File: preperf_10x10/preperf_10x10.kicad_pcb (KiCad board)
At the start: 2 copper layers, 100 x 100 mm, 72 parts, among them J1 Conn_01x02_Pin, J2 Conn_01x02_Pin, J3 Conn_01x02_Pin, J4 Conn_01x01_Pin, J5 Conn_01x01_Pin, J6 Conn_01x01_Pin, J7 Conn_01x01_Pin, J8 Conn_01x01_Pin, J9 Conn_01x01_Pin, Q1 BC548, Q2 BC558, SW1 SW_DIP_x06, SW2 SW_Push, U1 LM7805_TO220, U10 74LS14, U11 74LS73, U12 74LS73, U13 74LS08, U14 74LS32, U2 74LS08, U3 74LS32, U4 74LS04, U5 74LS02, U6 7400, U7 74LS86, U8 4511, U9 D168K

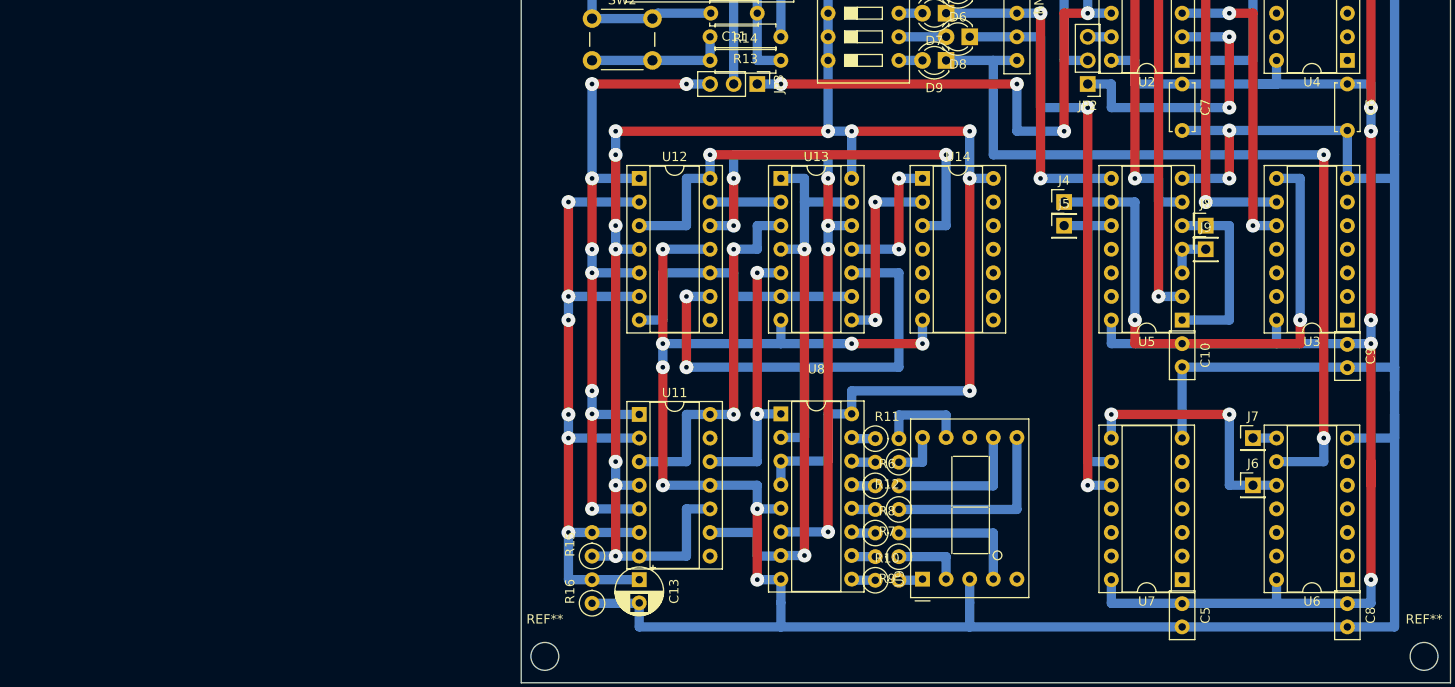
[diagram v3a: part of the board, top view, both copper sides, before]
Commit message: Fix BCD UP counter
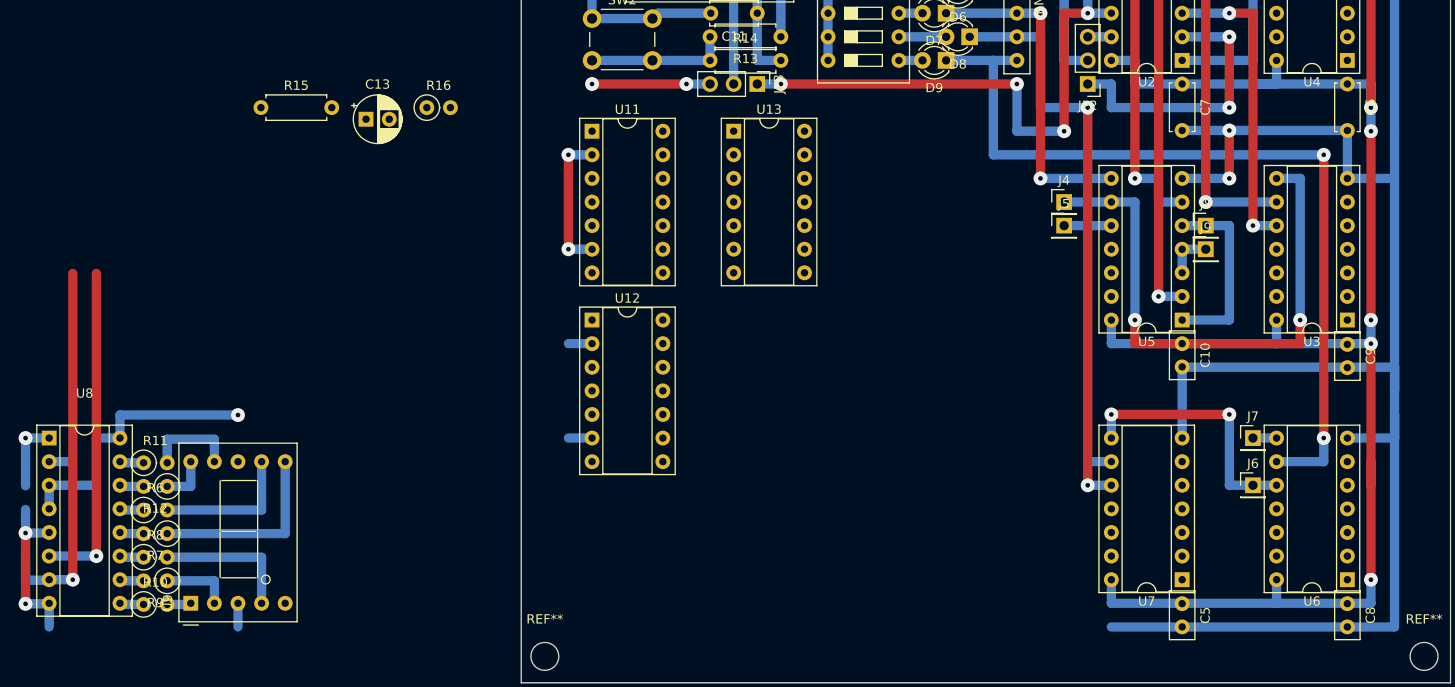
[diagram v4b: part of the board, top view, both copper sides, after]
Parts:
- removed U14: 74LS32, Package_DIP:DIP-14_W7.62mm_Socket
- R15: footprint Resistor_THT:R_Axial_DIN0207_L6.3mm_D2.5mm_P2.54mm_Vertical -> Resistor_THT:R_Axial_DIN0207_L6.3mm_D2.5mm_P7.62mm_Horizontal
- moved U8 78.8 mm to (48.3, 119.4)
- moved U9 78.8 mm to (63.5, 137.2)
- moved R10 78.8 mm to (58.4, 137.3)
- moved R11 78.8 mm to (58.4, 122.0)
- moved R6 78.8 mm to (58.4, 127.1)
- moved R8 78.8 mm to (58.4, 132.2)
- moved R12 78.8 mm to (61.0, 124.6)
- moved R7 78.8 mm to (61.0, 129.7)
- moved R9 78.8 mm to (61.0, 134.7)
- moved R15 60.0 mm to (71.0, 83.8), turned to 0 degrees
- moved C13 57.6 mm to (82.4, 85.1), turned to 0 degrees
- moved R16 56.2 mm to (88.9, 83.8), turned to 0 degrees
- moved U11 30.9 mm to (106.7, 86.4)
- moved U12 16.1 mm to (106.7, 106.7)
- moved U13 7.19 mm to (121.9, 86.4)
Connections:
- U11 pad 12: /Contador BCD UP/Q_{B} -> /Contador BCD UP/Q_{1}
- U11 pad 14: Net-(U11B-J) -> /Contador BCD UP/J_{1}
- U11 pad 3: Net-(U11B-J) -> /Contador BCD UP/Q_{0}
- U11 pad 9: /Contador BCD UP/Q_{A} -> /Contador BCD UP/Q_{0}
- U12 pad 10: Net-(U12A-J) -> /Contador BCD UP/J_{2}
- U12 pad 12: /Contador BCD UP/Q_{D} -> /Contador BCD UP/Q_{3}
- U12 pad 13: Net-(U12B-~{Q}) -> /Contador BCD UP/~{Q_{3}}
- U12 pad 14: Net-(U12B-J) -> /Contador BCD UP/J_{3}
- U12 pad 3: Net-(U12B-J) -> /Contador BCD UP/Q_{0}
- U12 pad 7: Net-(U12A-J) -> /Contador BCD UP/J_{2}
- U12 pad 9: /Contador BCD UP/Q_{C} -> /Contador BCD UP/Q_{2}
- U13 pad 1: /Contador BCD UP/Q_{A} -> /Contador BCD UP/Q_{1}
- U13 pad 10: /Contador BCD UP/Q_{C} -> /Contador BCD UP/~{Q_{3}}
- U13 pad 11: Net-(U13-Pad11) -> unconnected-(U13-Pad11)
- U13 pad 12: /Contador BCD UP/Q_{D} -> unconnected-(U13-Pad12)
- U13 pad 13: /Contador BCD UP/Q_{A} -> unconnected-(U13-Pad13)
- U13 pad 2: Net-(U12B-~{Q}) -> /Contador BCD UP/Q_{0}
- U13 pad 3: Net-(U11B-J) -> /Contador BCD UP/J_{2}
- U13 pad 4: /Contador BCD UP/Q_{A} -> /Contador BCD UP/Q_{2}
- U13 pad 5: /Contador BCD UP/Q_{B} -> /Contador BCD UP/J_{2}
- U13 pad 6: Net-(U12A-J) -> /Contador BCD UP/J_{3}
- U13 pad 8: Net-(U13-Pad8) -> /Contador BCD UP/J_{1}
- U13 pad 9: Net-(U12A-J) -> /Contador BCD UP/Q_{0}
- U8 pad 1: /Contador BCD UP/Q_{B} -> /Contador BCD UP/Q_{1}
- U8 pad 2: /Contador BCD UP/Q_{C} -> /Contador BCD UP/Q_{2}
- U8 pad 6: /Contador BCD UP/Q_{D} -> /Contador BCD UP/Q_{3}
- U8 pad 7: /Contador BCD UP/Q_{A} -> /Contador BCD UP/Q_{0}
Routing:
- net +5V: track 505.3 -> 355.4 mm, vias 23 -> 12
- net GND: track 514.6 -> 377.3 mm, vias 14 -> 8
- net /Contador BCD UP/Q_{D}: track 68.5 -> 0.00 mm, vias 6 -> 0
- net /Contador BCD UP/CLK: track 78.8 -> 12.7 mm, vias 8 -> 2
- net /Contador BCD UP/Q_{A}: track 63.7 -> 0.00 mm, vias 2 -> 0
- net /Contador BCD UP/POR: track 78.7 -> 20.3 mm, vias 6 -> 2
- net /Contador BCD UP/Q_{C}: track 58.4 -> 0.00 mm, vias 2 -> 0
- net Net-(U12B-J): track 50.8 -> 0.00 mm, vias 2 -> 0
- net /Contador BCD UP/Q_{0}: track 0.00 -> 40.8 mm, vias 0 -> 1
- net Net-(U11B-J): track 40.6 -> 0.00 mm, vias 2 -> 0
- net /Contador BCD UP/Q_{3}: track 0.00 -> 35.5 mm, vias 0 -> 1
- net /Contador BCD UP/Q_{B}: track 30.6 -> 0.00 mm, vias 2 -> 0
- net Net-(U12A-J): track 30.5 -> 0.00 mm
- net Net-(U13-Pad8): track 20.3 -> 0.00 mm, vias 2 -> 0
- net Net-(U13-Pad11): track 15.2 -> 0.00 mm, vias 2 -> 0
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
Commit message: [ADD] Digital Logic Design project (FIUBA): PCB implementation of schmitt triggers, logic functions, counters, state machines, and logic probes
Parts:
- removed the REF** at (101.6, 142.9)
- removed the REF** at (196.2, 48.3)
- removed the REF** at (196.2, 142.9)
- removed the REF** at (101.6, 48.3)
- added 10: , , F.Cu at (183.2, 54.9)
- added 1022: , , F.Cu at (162.9, 98.1)
- added 1023: , , F.Cu at (165.4, 98.1)
- added 1024: , , F.Cu at (167.9, 98.1)
- added 1025: , , F.Cu at (170.5, 98.1)
- added 1026: , , F.Cu at (173.0, 98.1)
- added 1027: , , F.Cu at (175.6, 98.1)
- added 1028: , , F.Cu at (178.1, 98.1)
- added 1029: , , F.Cu at (180.6, 98.1)
- added 1030: , , F.Cu at (183.2, 98.1)
- added 1031: , , F.Cu at (185.7, 98.1)
- added 1032: , , F.Cu at (188.3, 98.1)
- added 1033: , , F.Cu at (190.8, 98.1)
- added 1034: , , F.Cu at (193.3, 98.1)
- added 1035: , , F.Cu at (195.9, 98.1)
- added 1036: , , F.Cu at (198.4, 98.1)
- added 1037: , , F.Cu at (201.0, 98.1)
- added 1038: , , F.Cu at (203.5, 98.1)
- added 1039: , , F.Cu at (206.0, 98.1)
- added 1040: , , F.Cu at (208.6, 98.1)
- added 1041: , , F.Cu at (211.1, 98.1)
- added 1042: , , F.Cu at (213.7, 98.1)
- added 1043: , , F.Cu at (216.2, 98.1)
- added 1044: , , F.Cu at (218.7, 98.1)
- added 1045: , , F.Cu at (221.3, 98.1)
- added 1046: , , F.Cu at (223.8, 98.1)
- added 1047: , , F.Cu at (226.4, 98.1)
- added 1048: , , F.Cu at (228.9, 98.1)
- added 1049: , , F.Cu at (231.4, 98.1)
- added 1050: , , F.Cu at (234.0, 98.1)
- added 1051: , , F.Cu at (236.5, 98.1)
- added 1052: , , F.Cu at (239.1, 98.1)
- added 1053: , , F.Cu at (241.6, 98.1)
- added 1054: , , F.Cu at (244.1, 98.1)
- added 1055: , , F.Cu at (246.7, 98.1)
- added 1056: , , F.Cu at (249.2, 98.1)
- added 1057: , , F.Cu at (251.8, 98.1)
- added 1082: , , F.Cu at (162.9, 100.6)
- added 1083: , , F.Cu at (165.4, 100.6)
- added 1084: , , F.Cu at (167.9, 100.6)
- added 1085: , , F.Cu at (170.5, 100.6)
- added 1086: , , F.Cu at (173.0, 100.6)
- added 1087: , , F.Cu at (175.6, 100.6)
- added 1088: , , F.Cu at (178.1, 100.6)
- added 1089: , , F.Cu at (180.6, 100.6)
- added 1090: , , F.Cu at (183.2, 100.6)
- added 1091: , , F.Cu at (185.7, 100.6)
- added 1092: , , F.Cu at (188.3, 100.6)
- added 1093: , , F.Cu at (190.8, 100.6)
- added 1094: , , F.Cu at (193.3, 100.6)
- added 1095: , , F.Cu at (195.9, 100.6)
- added 1096: , , F.Cu at (198.4, 100.6)
- added 1097: , , F.Cu at (201.0, 100.6)
- added 1098: , , F.Cu at (203.5, 100.6)
- added 1099: , , F.Cu at (206.0, 100.6)
- added 11: , , F.Cu at (185.7, 54.9)
- added 1100: , , F.Cu at (208.6, 100.6)
- added 1101: , , F.Cu at (211.1, 100.6)
- added 1102: , , F.Cu at (213.7, 100.6)
- added 1103: , , F.Cu at (216.2, 100.6)
- added 1104: , , F.Cu at (218.7, 100.6)
- added 1105: , , F.Cu at (221.3, 100.6)
- added 1106: , , F.Cu at (223.8, 100.6)
- added 1107: , , F.Cu at (226.4, 100.6)
- added 1108: , , F.Cu at (228.9, 100.6)
- added 1109: , , F.Cu at (231.4, 100.6)
- added 1110: , , F.Cu at (234.0, 100.6)
- added 1111: , , F.Cu at (236.5, 100.6)
- added 1112: , , F.Cu at (239.1, 100.6)
- added 1113: , , F.Cu at (241.6, 100.6)
- added 1114: , , F.Cu at (244.1, 100.6)
- added 1115: , , F.Cu at (246.7, 100.6)
- added 1116: , , F.Cu at (249.2, 100.6)
- added 1117: , , F.Cu at (251.8, 100.6)
- added 1142: , , F.Cu at (162.9, 103.2)
- added 1143: , , F.Cu at (165.4, 103.2)
- added 1144: , , F.Cu at (167.9, 103.2)
- added 1145: , , F.Cu at (170.5, 103.2)
- added 1146: , , F.Cu at (173.0, 103.2)
- added 1147: , , F.Cu at (175.6, 103.2)
- added 1148: , , F.Cu at (178.1, 103.2)
- added 1149: , , F.Cu at (180.6, 103.2)
- added 1150: , , F.Cu at (183.2, 103.2)
- added 1151: , , F.Cu at (185.7, 103.2)
- added 1152: , , F.Cu at (188.3, 103.2)
- added 1153: , , F.Cu at (190.8, 103.2)
- added 1154: , , F.Cu at (193.3, 103.2)
- added 1155: , , F.Cu at (195.9, 103.2)
- added 1156: , , F.Cu at (198.4, 103.2)
- added 1157: , , F.Cu at (201.0, 103.2)
- added 1158: , , F.Cu at (203.5, 103.2)
- added 1159: , , F.Cu at (206.0, 103.2)
- added 1160: , , F.Cu at (208.6, 103.2)
- added 1161: , , F.Cu at (211.1, 103.2)
- added 1162: , , F.Cu at (213.7, 103.2)
- added 1163: , , F.Cu at (216.2, 103.2)
- added 1164: , , F.Cu at (218.7, 103.2)
- added 1165: , , F.Cu at (221.3, 103.2)
- added 1166: , , F.Cu at (223.8, 103.2)
- added 1167: , , F.Cu at (226.4, 103.2)
- added 1168: , , F.Cu at (228.9, 103.2)
- added 1169: , , F.Cu at (231.4, 103.2)
- added 1170: , , F.Cu at (234.0, 103.2)
- added 1171: , , F.Cu at (236.5, 103.2)
- added 1172: , , F.Cu at (239.1, 103.2)
- added 1173: , , F.Cu at (241.6, 103.2)
- added 1174: , , F.Cu at (244.1, 103.2)
- added 1175: , , F.Cu at (246.7, 103.2)
- added 1176: , , F.Cu at (249.2, 103.2)
- added 1177: , , F.Cu at (251.8, 103.2)
- added 12: , , F.Cu at (188.3, 54.9)
- added 1202: , , F.Cu at (162.9, 105.7)
- added 1203: , , F.Cu at (165.4, 105.7)
- added 1204: , , F.Cu at (167.9, 105.7)
- added 1205: , , F.Cu at (170.5, 105.7)
- added 1206: , , F.Cu at (173.0, 105.7)
- added 1207: , , F.Cu at (175.6, 105.7)
- added 1208: , , F.Cu at (178.1, 105.7)
- added 1209: , , F.Cu at (180.6, 105.7)
- added 1210: , , F.Cu at (183.2, 105.7)
- added 1211: , , F.Cu at (185.7, 105.7)
- added 1212: , , F.Cu at (188.3, 105.7)
- added 1213: , , F.Cu at (190.8, 105.7)
- added 1214: , , F.Cu at (193.3, 105.7)
- added 1215: , , F.Cu at (195.9, 105.7)
- added 1216: , , F.Cu at (198.4, 105.7)
- added 1217: , , F.Cu at (201.0, 105.7)
- added 1218: , , F.Cu at (203.5, 105.7)
- added 1219: , , F.Cu at (206.0, 105.7)
- added 122: , , F.Cu at (162.9, 60.0)
- added 1220: , , F.Cu at (208.6, 105.7)
- added 1221: , , F.Cu at (211.1, 105.7)
- added 1222: , , F.Cu at (213.7, 105.7)
- added 1223: , , F.Cu at (216.2, 105.7)
- added 1224: , , F.Cu at (218.7, 105.7)
- added 1225: , , F.Cu at (221.3, 105.7)
- added 1226: , , F.Cu at (223.8, 105.7)
- added 1227: , , F.Cu at (226.4, 105.7)
- added 1228: , , F.Cu at (228.9, 105.7)
- added 1229: , , F.Cu at (231.4, 105.7)
- added 123: , , F.Cu at (165.4, 60.0)
- added 1230: , , F.Cu at (234.0, 105.7)
- added 1231: , , F.Cu at (236.5, 105.7)
- added 1232: , , F.Cu at (239.1, 105.7)
- added 1233: , , F.Cu at (241.6, 105.7)
- added 1234: , , F.Cu at (244.1, 105.7)
- added 1235: , , F.Cu at (246.7, 105.7)
- added 1236: , , F.Cu at (249.2, 105.7)
- added 1237: , , F.Cu at (251.8, 105.7)
- added 124: , , F.Cu at (167.9, 60.0)
- added 125: , , F.Cu at (170.5, 60.0)
- added 126: , , F.Cu at (173.0, 60.0)
- added 1262: , , F.Cu at (162.9, 108.2)
- added 1263: , , F.Cu at (165.4, 108.2)
- added 1264: , , F.Cu at (167.9, 108.2)
- added 1265: , , F.Cu at (170.5, 108.2)
- added 1266: , , F.Cu at (173.0, 108.2)
- added 1267: , , F.Cu at (175.6, 108.2)
- added 1268: , , F.Cu at (178.1, 108.2)
- added 1269: , , F.Cu at (180.6, 108.2)
- added 127: , , F.Cu at (175.6, 60.0)
- added 1270: , , F.Cu at (183.2, 108.2)
- added 1271: , , F.Cu at (185.7, 108.2)
- added 1272: , , F.Cu at (188.3, 108.2)
- added 1273: , , F.Cu at (190.8, 108.2)
- added 1274: , , F.Cu at (193.3, 108.2)
- added 1275: , , F.Cu at (195.9, 108.2)
- added 1276: , , F.Cu at (198.4, 108.2)
- added 1277: , , F.Cu at (201.0, 108.2)
- added 1278: , , F.Cu at (203.5, 108.2)
- added 1279: , , F.Cu at (206.0, 108.2)
- added 128: , , F.Cu at (178.1, 60.0)
- added 1280: , , F.Cu at (208.6, 108.2)
- added 1281: , , F.Cu at (211.1, 108.2)
- added 1282: , , F.Cu at (213.7, 108.2)
- added 1283: , , F.Cu at (216.2, 108.2)
- added 1284: , , F.Cu at (218.7, 108.2)
- added 1285: , , F.Cu at (221.3, 108.2)
- added 1286: , , F.Cu at (223.8, 108.2)
- added 1287: , , F.Cu at (226.4, 108.2)
- added 1288: , , F.Cu at (228.9, 108.2)
- added 1289: , , F.Cu at (231.4, 108.2)
- added 129: , , F.Cu at (180.6, 60.0)
- added 1290: , , F.Cu at (234.0, 108.2)
- added 1291: , , F.Cu at (236.5, 108.2)
- added 1292: , , F.Cu at (239.1, 108.2)
- added 1293: , , F.Cu at (241.6, 108.2)
- added 1294: , , F.Cu at (244.1, 108.2)
- added 1295: , , F.Cu at (246.7, 108.2)
- added 1296: , , F.Cu at (249.2, 108.2)
- added 1297: , , F.Cu at (251.8, 108.2)
- added 13: , , F.Cu at (190.8, 54.9)
- added 130: , , F.Cu at (183.2, 60.0)
- added 131: , , F.Cu at (185.7, 60.0)
- added 132: , , F.Cu at (188.3, 60.0)
- added 1322: , , F.Cu at (162.9, 110.8)
- added 1323: , , F.Cu at (165.4, 110.8)
- added 1324: , , F.Cu at (167.9, 110.8)
- added 1325: , , F.Cu at (170.5, 110.8)
- added 1326: , , F.Cu at (173.0, 110.8)
- added 1327: , , F.Cu at (175.6, 110.8)
- added 1328: , , F.Cu at (178.1, 110.8)
- added 1329: , , F.Cu at (180.6, 110.8)
- added 133: , , F.Cu at (190.8, 60.0)
- added 1330: , , F.Cu at (183.2, 110.8)
- added 1331: , , F.Cu at (185.7, 110.8)
- added 1332: , , F.Cu at (188.3, 110.8)
- added 1333: , , F.Cu at (190.8, 110.8)
- added 1334: , , F.Cu at (193.3, 110.8)
- added 1335: , , F.Cu at (195.9, 110.8)
- added 1336: , , F.Cu at (198.4, 110.8)
- added 1337: , , F.Cu at (201.0, 110.8)
- added 1338: , , F.Cu at (203.5, 110.8)
- added 1339: , , F.Cu at (206.0, 110.8)
- added 134: , , F.Cu at (193.3, 60.0)
- added 1340: , , F.Cu at (208.6, 110.8)
- added 1341: , , F.Cu at (211.1, 110.8)
- added 1342: , , F.Cu at (213.7, 110.8)
- added 1343: , , F.Cu at (216.2, 110.8)
- added 1344: , , F.Cu at (218.7, 110.8)
- added 1345: , , F.Cu at (221.3, 110.8)
- added 1346: , , F.Cu at (223.8, 110.8)
- added 1347: , , F.Cu at (226.4, 110.8)
- added 1348: , , F.Cu at (228.9, 110.8)
- added 1349: , , F.Cu at (231.4, 110.8)
- added 135: , , F.Cu at (195.9, 60.0)
- added 1350: , , F.Cu at (234.0, 110.8)
- added 1351: , , F.Cu at (236.5, 110.8)
- added 1352: , , F.Cu at (239.1, 110.8)
- added 1353: , , F.Cu at (241.6, 110.8)
- added 1354: , , F.Cu at (244.1, 110.8)
- added 1355: , , F.Cu at (246.7, 110.8)
- added 1356: , , F.Cu at (249.2, 110.8)
- added 1357: , , F.Cu at (251.8, 110.8)
- added 136: , , F.Cu at (198.4, 60.0)
- added 137: , , F.Cu at (201.0, 60.0)
- added 138: , , F.Cu at (203.5, 60.0)
- added 1382: , , F.Cu at (162.9, 113.3)
- added 1383: , , F.Cu at (165.4, 113.3)
- added 1384: , , F.Cu at (167.9, 113.3)
- added 1385: , , F.Cu at (170.5, 113.3)
- added 1386: , , F.Cu at (173.0, 113.3)
- added 1387: , , F.Cu at (175.6, 113.3)
- added 1388: , , F.Cu at (178.1, 113.3)
- added 1389: , , F.Cu at (180.6, 113.3)
- added 139: , , F.Cu at (206.0, 60.0)
- added 1390: , , F.Cu at (183.2, 113.3)
- added 1391: , , F.Cu at (185.7, 113.3)
- added 1392: , , F.Cu at (188.3, 113.3)
- added 1393: , , F.Cu at (190.8, 113.3)
- added 1394: , , F.Cu at (193.3, 113.3)
- added 1395: , , F.Cu at (195.9, 113.3)
- added 1396: , , F.Cu at (198.4, 113.3)
- added 1397: , , F.Cu at (201.0, 113.3)
- added 1398: , , F.Cu at (203.5, 113.3)
- added 1399: , , F.Cu at (206.0, 113.3)
- added 14: , , F.Cu at (193.3, 54.9)
- added 140: , , F.Cu at (208.6, 60.0)
- added 1400: , , F.Cu at (208.6, 113.3)
- added 1401: , , F.Cu at (211.1, 113.3)
- added 1402: , , F.Cu at (213.7, 113.3)
- added 1403: , , F.Cu at (216.2, 113.3)
- added 1404: , , F.Cu at (218.7, 113.3)
- added 1405: , , F.Cu at (221.3, 113.3)
- added 1406: , , F.Cu at (223.8, 113.3)
- added 1407: , , F.Cu at (226.4, 113.3)
- added 1408: , , F.Cu at (228.9, 113.3)
- added 1409: , , F.Cu at (231.4, 113.3)
- added 141: , , F.Cu at (211.1, 60.0)
- added 1410: , , F.Cu at (234.0, 113.3)
- added 1411: , , F.Cu at (236.5, 113.3)
- added 1412: , , F.Cu at (239.1, 113.3)
- added 1413: , , F.Cu at (241.6, 113.3)
- added 1414: , , F.Cu at (244.1, 113.3)
- added 1415: , , F.Cu at (246.7, 113.3)
- added 1416: , , F.Cu at (249.2, 113.3)
- added 1417: , , F.Cu at (251.8, 113.3)
- added 142: , , F.Cu at (213.7, 60.0)
- added 143: , , F.Cu at (216.2, 60.0)
- added 144: , , F.Cu at (218.7, 60.0)
- added 1442: , , F.Cu at (162.9, 115.9)
- added 1443: , , F.Cu at (165.4, 115.9)
- added 1444: , , F.Cu at (167.9, 115.9)
- added 1445: , , F.Cu at (170.5, 115.9)
- added 1446: , , F.Cu at (173.0, 115.9)
- added 1447: , , F.Cu at (175.6, 115.9)
- added 1448: , , F.Cu at (178.1, 115.9)
- added 1449: , , F.Cu at (180.6, 115.9)
- added 145: , , F.Cu at (221.3, 60.0)
- added 1450: , , F.Cu at (183.2, 115.9)
- added 1451: , , F.Cu at (185.7, 115.9)
- added 1452: , , F.Cu at (188.3, 115.9)
- added 1453: , , F.Cu at (190.8, 115.9)
- added 1454: , , F.Cu at (193.3, 115.9)
- added 1455: , , F.Cu at (195.9, 115.9)
- added 1456: , , F.Cu at (198.4, 115.9)
- added 1457: , , F.Cu at (201.0, 115.9)
- added 1458: , , F.Cu at (203.5, 115.9)
- added 1459: , , F.Cu at (206.0, 115.9)
- added 146: , , F.Cu at (223.8, 60.0)
- added 1460: , , F.Cu at (208.6, 115.9)
- added 1461: , , F.Cu at (211.1, 115.9)
- added 1462: , , F.Cu at (213.7, 115.9)
- added 1463: , , F.Cu at (216.2, 115.9)
- added 1464: , , F.Cu at (218.7, 115.9)
- added 1465: , , F.Cu at (221.3, 115.9)
- added 1466: , , F.Cu at (223.8, 115.9)
- added 1467: , , F.Cu at (226.4, 115.9)
- added 1468: , , F.Cu at (228.9, 115.9)
- added 1469: , , F.Cu at (231.4, 115.9)
- added 147: , , F.Cu at (226.4, 60.0)
- added 1470: , , F.Cu at (234.0, 115.9)
- added 1471: , , F.Cu at (236.5, 115.9)
- added 1472: , , F.Cu at (239.1, 115.9)
- added 1473: , , F.Cu at (241.6, 115.9)
- added 1474: , , F.Cu at (244.1, 115.9)
- added 1475: , , F.Cu at (246.7, 115.9)
- added 1476: , , F.Cu at (249.2, 115.9)
- added 1477: , , F.Cu at (251.8, 115.9)
- added 148: , , F.Cu at (228.9, 60.0)
- added 149: , , F.Cu at (231.4, 60.0)
- added 15: , , F.Cu at (195.9, 54.9)
- added 150: , , F.Cu at (234.0, 60.0)
- added 1502: , , F.Cu at (162.9, 118.4)
- added 1503: , , F.Cu at (165.4, 118.4)
- added 1504: , , F.Cu at (167.9, 118.4)
- added 1505: , , F.Cu at (170.5, 118.4)
- added 1506: , , F.Cu at (173.0, 118.4)
- added 1507: , , F.Cu at (175.6, 118.4)
- added 1508: , , F.Cu at (178.1, 118.4)
- added 1509: , , F.Cu at (180.6, 118.4)
- added 151: , , F.Cu at (236.5, 60.0)
- added 1510: , , F.Cu at (183.2, 118.4)
- added 1511: , , F.Cu at (185.7, 118.4)
- added 1512: , , F.Cu at (188.3, 118.4)
- added 1513: , , F.Cu at (190.8, 118.4)
- added 1514: , , F.Cu at (193.3, 118.4)
- added 1515: , , F.Cu at (195.9, 118.4)
- added 1516: , , F.Cu at (198.4, 118.4)
- added 1517: , , F.Cu at (201.0, 118.4)
- added 1518: , , F.Cu at (203.5, 118.4)
- added 1519: , , F.Cu at (206.0, 118.4)
- added 152: , , F.Cu at (239.1, 60.0)
- added 1520: , , F.Cu at (208.6, 118.4)
- added 1521: , , F.Cu at (211.1, 118.4)
- added 1522: , , F.Cu at (213.7, 118.4)
- added 1523: , , F.Cu at (216.2, 118.4)
- added 1524: , , F.Cu at (218.7, 118.4)
- added 1525: , , F.Cu at (221.3, 118.4)
- added 1526: , , F.Cu at (223.8, 118.4)
- added 1527: , , F.Cu at (226.4, 118.4)
- added 1528: , , F.Cu at (228.9, 118.4)
- added 1529: , , F.Cu at (231.4, 118.4)
- added 153: , , F.Cu at (241.6, 60.0)
- added 1530: , , F.Cu at (234.0, 118.4)
- added 1531: , , F.Cu at (236.5, 118.4)
- added 1532: , , F.Cu at (239.1, 118.4)
- added 1533: , , F.Cu at (241.6, 118.4)
- added 1534: , , F.Cu at (244.1, 118.4)
- added 1535: , , F.Cu at (246.7, 118.4)
- added 1536: , , F.Cu at (249.2, 118.4)
- added 1537: , , F.Cu at (251.8, 118.4)
- added 154: , , F.Cu at (244.1, 60.0)
- added 155: , , F.Cu at (246.7, 60.0)
- added 156: , , F.Cu at (249.2, 60.0)
- added 1562: , , F.Cu at (162.9, 120.9)
- added 1563: , , F.Cu at (165.4, 120.9)
- added 1564: , , F.Cu at (167.9, 120.9)
- added 1565: , , F.Cu at (170.5, 120.9)
- added 1566: , , F.Cu at (173.0, 120.9)
- added 1567: , , F.Cu at (175.6, 120.9)
- added 1568: , , F.Cu at (178.1, 120.9)
- added 1569: , , F.Cu at (180.6, 120.9)
- added 157: , , F.Cu at (251.8, 60.0)
- added 1570: , , F.Cu at (183.2, 120.9)
- added 1571: , , F.Cu at (185.7, 120.9)
- added 1572: , , F.Cu at (188.3, 120.9)
- added 1573: , , F.Cu at (190.8, 120.9)
- added 1574: , , F.Cu at (193.3, 120.9)
- added 1575: , , F.Cu at (195.9, 120.9)
- added 1576: , , F.Cu at (198.4, 120.9)
- added 1577: , , F.Cu at (201.0, 120.9)
- added 1578: , , F.Cu at (203.5, 120.9)
- added 1579: , , F.Cu at (206.0, 120.9)
- added 1580: , , F.Cu at (208.6, 120.9)
- added 1581: , , F.Cu at (211.1, 120.9)
- added 1582: , , F.Cu at (213.7, 120.9)
- added 1583: , , F.Cu at (216.2, 120.9)
- added 1584: , , F.Cu at (218.7, 120.9)
- added 1585: , , F.Cu at (221.3, 120.9)
- added 1586: , , F.Cu at (223.8, 120.9)
- added 1587: , , F.Cu at (226.4, 120.9)
- added 1588: , , F.Cu at (228.9, 120.9)
- added 1589: , , F.Cu at (231.4, 120.9)
- added 1590: , , F.Cu at (234.0, 120.9)
- added 1591: , , F.Cu at (236.5, 120.9)
- added 1592: , , F.Cu at (239.1, 120.9)
- added 1593: , , F.Cu at (241.6, 120.9)
- added 1594: , , F.Cu at (244.1, 120.9)
- added 1595: , , F.Cu at (246.7, 120.9)
- added 1596: , , F.Cu at (249.2, 120.9)
- added 1597: , , F.Cu at (251.8, 120.9)
- added 16: , , F.Cu at (198.4, 54.9)
- added 1622: , , F.Cu at (162.9, 123.5)
- added 1623: , , F.Cu at (165.4, 123.5)
- added 1624: , , F.Cu at (167.9, 123.5)
- added 1625: , , F.Cu at (170.5, 123.5)
- added 1626: , , F.Cu at (173.0, 123.5)
- added 1627: , , F.Cu at (175.6, 123.5)
- added 1628: , , F.Cu at (178.1, 123.5)
- added 1629: , , F.Cu at (180.6, 123.5)
- added 1630: , , F.Cu at (183.2, 123.5)
- added 1631: , , F.Cu at (185.7, 123.5)
- added 1632: , , F.Cu at (188.3, 123.5)
- added 1633: , , F.Cu at (190.8, 123.5)
- added 1634: , , F.Cu at (193.3, 123.5)
- added 1635: , , F.Cu at (195.9, 123.5)
- added 1636: , , F.Cu at (198.4, 123.5)
- added 1637: , , F.Cu at (201.0, 123.5)
- added 1638: , , F.Cu at (203.5, 123.5)
- added 1639: , , F.Cu at (206.0, 123.5)
- added 1640: , , F.Cu at (208.6, 123.5)
- added 1641: , , F.Cu at (211.1, 123.5)
- added 1642: , , F.Cu at (213.7, 123.5)
- added 1643: , , F.Cu at (216.2, 123.5)
- added 1644: , , F.Cu at (218.7, 123.5)
- added 1645: , , F.Cu at (221.3, 123.5)
- added 1646: , , F.Cu at (223.8, 123.5)
- added 1647: , , F.Cu at (226.4, 123.5)
- added 1648: , , F.Cu at (228.9, 123.5)
- added 1649: , , F.Cu at (231.4, 123.5)
- added 1650: , , F.Cu at (234.0, 123.5)
- added 1651: , , F.Cu at (236.5, 123.5)
- added 1652: , , F.Cu at (239.1, 123.5)
- added 1653: , , F.Cu at (241.6, 123.5)
- added 1654: , , F.Cu at (244.1, 123.5)
- added 1655: , , F.Cu at (246.7, 123.5)
- added 1656: , , F.Cu at (249.2, 123.5)
- added 1657: , , F.Cu at (251.8, 123.5)
- added 1682: , , F.Cu at (162.9, 126.0)
- added 1683: , , F.Cu at (165.4, 126.0)
- added 1684: , , F.Cu at (167.9, 126.0)
- added 1685: , , F.Cu at (170.5, 126.0)
- added 1686: , , F.Cu at (173.0, 126.0)
- added 1687: , , F.Cu at (175.6, 126.0)
- added 1688: , , F.Cu at (178.1, 126.0)
- added 1689: , , F.Cu at (180.6, 126.0)
- added 1690: , , F.Cu at (183.2, 126.0)
- added 1691: , , F.Cu at (185.7, 126.0)
- added 1692: , , F.Cu at (188.3, 126.0)
- added 1693: , , F.Cu at (190.8, 126.0)
- added 1694: , , F.Cu at (193.3, 126.0)
- added 1695: , , F.Cu at (195.9, 126.0)
- added 1696: , , F.Cu at (198.4, 126.0)
- added 1697: , , F.Cu at (201.0, 126.0)
- added 1698: , , F.Cu at (203.5, 126.0)
- added 1699: , , F.Cu at (206.0, 126.0)
- added 17: , , F.Cu at (201.0, 54.9)
- added 1700: , , F.Cu at (208.6, 126.0)
- added 1701: , , F.Cu at (211.1, 126.0)
- added 1702: , , F.Cu at (213.7, 126.0)
- added 1703: , , F.Cu at (216.2, 126.0)
- added 1704: , , F.Cu at (218.7, 126.0)
- added 1705: , , F.Cu at (221.3, 126.0)
- added 1706: , , F.Cu at (223.8, 126.0)
- added 1707: , , F.Cu at (226.4, 126.0)
- added 1708: , , F.Cu at (228.9, 126.0)
- added 1709: , , F.Cu at (231.4, 126.0)
- added 1710: , , F.Cu at (234.0, 126.0)
- added 1711: , , F.Cu at (236.5, 126.0)
- added 1712: , , F.Cu at (239.1, 126.0)
- added 1713: , , F.Cu at (241.6, 126.0)
- added 1714: , , F.Cu at (244.1, 126.0)
- added 1715: , , F.Cu at (246.7, 126.0)
- added 1716: , , F.Cu at (249.2, 126.0)
- added 1717: , , F.Cu at (251.8, 126.0)
- added 1742: , , F.Cu at (162.9, 128.6)
- added 1743: , , F.Cu at (165.4, 128.6)
- added 1744: , , F.Cu at (167.9, 128.6)
- added 1745: , , F.Cu at (170.5, 128.6)
- added 1746: , , F.Cu at (173.0, 128.6)
- added 1747: , , F.Cu at (175.6, 128.6)
- added 1748: , , F.Cu at (178.1, 128.6)
- added 1749: , , F.Cu at (180.6, 128.6)
- added 1750: , , F.Cu at (183.2, 128.6)
- added 1751: , , F.Cu at (185.7, 128.6)
- added 1752: , , F.Cu at (188.3, 128.6)
- added 1753: , , F.Cu at (190.8, 128.6)
- added 1754: , , F.Cu at (193.3, 128.6)
- added 1755: , , F.Cu at (195.9, 128.6)
- added 1756: , , F.Cu at (198.4, 128.6)
- added 1757: , , F.Cu at (201.0, 128.6)
- added 1758: , , F.Cu at (203.5, 128.6)
- added 1759: , , F.Cu at (206.0, 128.6)
- added 1760: , , F.Cu at (208.6, 128.6)
- added 1761: , , F.Cu at (211.1, 128.6)
- added 1762: , , F.Cu at (213.7, 128.6)
- added 1763: , , F.Cu at (216.2, 128.6)
- added 1764: , , F.Cu at (218.7, 128.6)
- added 1765: , , F.Cu at (221.3, 128.6)
- added 1766: , , F.Cu at (223.8, 128.6)
- added 1767: , , F.Cu at (226.4, 128.6)
- added 1768: , , F.Cu at (228.9, 128.6)
- added 1769: , , F.Cu at (231.4, 128.6)
- added 1770: , , F.Cu at (234.0, 128.6)
- added 1771: , , F.Cu at (236.5, 128.6)
- added 1772: , , F.Cu at (239.1, 128.6)
- added 1773: , , F.Cu at (241.6, 128.6)
- added 1774: , , F.Cu at (244.1, 128.6)
- added 1775: , , F.Cu at (246.7, 128.6)
- added 1776: , , F.Cu at (249.2, 128.6)
- added 1777: , , F.Cu at (251.8, 128.6)
- added 18: , , F.Cu at (203.5, 54.9)
- added 1802: , , F.Cu at (162.9, 131.1)
- added 1803: , , F.Cu at (165.4, 131.1)
- added 1804: , , F.Cu at (167.9, 131.1)
- added 1805: , , F.Cu at (170.5, 131.1)
- added 1806: , , F.Cu at (173.0, 131.1)
- added 1807: , , F.Cu at (175.6, 131.1)
- added 1808: , , F.Cu at (178.1, 131.1)
- added 1809: , , F.Cu at (180.6, 131.1)
- added 1810: , , F.Cu at (183.2, 131.1)
- added 1811: , , F.Cu at (185.7, 131.1)
- added 1812: , , F.Cu at (188.3, 131.1)
- added 1813: , , F.Cu at (190.8, 131.1)
- added 1814: , , F.Cu at (193.3, 131.1)
- added 1815: , , F.Cu at (195.9, 131.1)
- added 1816: , , F.Cu at (198.4, 131.1)
- added 1817: , , F.Cu at (201.0, 131.1)
- added 1818: , , F.Cu at (203.5, 131.1)
- added 1819: , , F.Cu at (206.0, 131.1)
- added 182: , , F.Cu at (162.9, 62.5)
- added 1820: , , F.Cu at (208.6, 131.1)
- added 1821: , , F.Cu at (211.1, 131.1)
- added 1822: , , F.Cu at (213.7, 131.1)
- added 1823: , , F.Cu at (216.2, 131.1)
- added 1824: , , F.Cu at (218.7, 131.1)
- added 1825: , , F.Cu at (221.3, 131.1)
- added 1826: , , F.Cu at (223.8, 131.1)
- added 1827: , , F.Cu at (226.4, 131.1)
- added 1828: , , F.Cu at (228.9, 131.1)
- added 1829: , , F.Cu at (231.4, 131.1)
- added 183: , , F.Cu at (165.4, 62.5)
- added 1830: , , F.Cu at (234.0, 131.1)
- added 1831: , , F.Cu at (236.5, 131.1)
- added 1832: , , F.Cu at (239.1, 131.1)
- added 1833: , , F.Cu at (241.6, 131.1)
- added 1834: , , F.Cu at (244.1, 131.1)
- added 1835: , , F.Cu at (246.7, 131.1)
- added 1836: , , F.Cu at (249.2, 131.1)
- added 1837: , , F.Cu at (251.8, 131.1)
- added 184: , , F.Cu at (167.9, 62.5)
- added 185: , , F.Cu at (170.5, 62.5)
- added 186: , , F.Cu at (173.0, 62.5)
- added 1862: , , F.Cu at (162.9, 133.6)
- added 1863: , , F.Cu at (165.4, 133.6)
- added 1864: , , F.Cu at (167.9, 133.6)
- added 1865: , , F.Cu at (170.5, 133.6)
- added 1866: , , F.Cu at (173.0, 133.6)
- added 1867: , , F.Cu at (175.6, 133.6)
- added 1868: , , F.Cu at (178.1, 133.6)
- added 1869: , , F.Cu at (180.6, 133.6)
- added 187: , , F.Cu at (175.6, 62.5)
- added 1870: , , F.Cu at (183.2, 133.6)
- added 1871: , , F.Cu at (185.7, 133.6)
- added 1872: , , F.Cu at (188.3, 133.6)
- added 1873: , , F.Cu at (190.8, 133.6)
- added 1874: , , F.Cu at (193.3, 133.6)
- added 1875: , , F.Cu at (195.9, 133.6)
- added 1876: , , F.Cu at (198.4, 133.6)
- added 1877: , , F.Cu at (201.0, 133.6)
- added 1878: , , F.Cu at (203.5, 133.6)
- added 1879: , , F.Cu at (206.0, 133.6)
- added 188: , , F.Cu at (178.1, 62.5)
- added 1880: , , F.Cu at (208.6, 133.6)
- added 1881: , , F.Cu at (211.1, 133.6)
- added 1882: , , F.Cu at (213.7, 133.6)
- added 1883: , , F.Cu at (216.2, 133.6)
- added 1884: , , F.Cu at (218.7, 133.6)
- added 1885: , , F.Cu at (221.3, 133.6)
- added 1886: , , F.Cu at (223.8, 133.6)
- added 1887: , , F.Cu at (226.4, 133.6)
- added 1888: , , F.Cu at (228.9, 133.6)
- added 1889: , , F.Cu at (231.4, 133.6)
- added 189: , , F.Cu at (180.6, 62.5)
- added 1890: , , F.Cu at (234.0, 133.6)
- added 1891: , , F.Cu at (236.5, 133.6)
- added 1892: , , F.Cu at (239.1, 133.6)
- added 1893: , , F.Cu at (241.6, 133.6)
- added 1894: , , F.Cu at (244.1, 133.6)
- added 1895: , , F.Cu at (246.7, 133.6)
- added 1896: , , F.Cu at (249.2, 133.6)
- added 1897: , , F.Cu at (251.8, 133.6)
- added 19: , , F.Cu at (206.0, 54.9)
- added 190: , , F.Cu at (183.2, 62.5)
- added 191: , , F.Cu at (185.7, 62.5)
- added 192: , , F.Cu at (188.3, 62.5)
- added 1922: , , F.Cu at (162.9, 136.2)
- added 1923: , , F.Cu at (165.4, 136.2)
- added 1924: , , F.Cu at (167.9, 136.2)
- added 1925: , , F.Cu at (170.5, 136.2)
- added 1926: , , F.Cu at (173.0, 136.2)
- added 1927: , , F.Cu at (175.6, 136.2)
- added 1928: , , F.Cu at (178.1, 136.2)
- added 1929: , , F.Cu at (180.6, 136.2)
- added 193: , , F.Cu at (190.8, 62.5)
- added 1930: , , F.Cu at (183.2, 136.2)
- added 1931: , , F.Cu at (185.7, 136.2)
- added 1932: , , F.Cu at (188.3, 136.2)
- added 1933: , , F.Cu at (190.8, 136.2)
- added 1934: , , F.Cu at (193.3, 136.2)
- added 1935: , , F.Cu at (195.9, 136.2)
- added 1936: , , F.Cu at (198.4, 136.2)
- added 1937: , , F.Cu at (201.0, 136.2)
- added 1938: , , F.Cu at (203.5, 136.2)
- added 1939: , , F.Cu at (206.0, 136.2)
- added 194: , , F.Cu at (193.3, 62.5)
- added 1940: , , F.Cu at (208.6, 136.2)
- added 1941: , , F.Cu at (211.1, 136.2)
- added 1942: , , F.Cu at (213.7, 136.2)
- added 1943: , , F.Cu at (216.2, 136.2)
- added 1944: , , F.Cu at (218.7, 136.2)
- added 1945: , , F.Cu at (221.3, 136.2)
- added 1946: , , F.Cu at (223.8, 136.2)
- added 1947: , , F.Cu at (226.4, 136.2)
- added 1948: , , F.Cu at (228.9, 136.2)
- added 1949: , , F.Cu at (231.4, 136.2)
- added 195: , , F.Cu at (195.9, 62.5)
- added 1950: , , F.Cu at (234.0, 136.2)
- added 1951: , , F.Cu at (236.5, 136.2)
- added 1952: , , F.Cu at (239.1, 136.2)
- added 1953: , , F.Cu at (241.6, 136.2)
- added 1954: , , F.Cu at (244.1, 136.2)
- added 1955: , , F.Cu at (246.7, 136.2)
- added 1956: , , F.Cu at (249.2, 136.2)
- added 1957: , , F.Cu at (251.8, 136.2)
- added 196: , , F.Cu at (198.4, 62.5)
- added 197: , , F.Cu at (201.0, 62.5)
- added 198: , , F.Cu at (203.5, 62.5)
- added 1982: , , F.Cu at (162.9, 138.7)
- added 1983: , , F.Cu at (165.4, 138.7)
- added 1984: , , F.Cu at (167.9, 138.7)
- added 1985: , , F.Cu at (170.5, 138.7)
- added 1986: , , F.Cu at (173.0, 138.7)
- added 1987: , , F.Cu at (175.6, 138.7)
- added 1988: , , F.Cu at (178.1, 138.7)
- added 1989: , , F.Cu at (180.6, 138.7)
- added 199: , , F.Cu at (206.0, 62.5)
- added 1990: , , F.Cu at (183.2, 138.7)
- added 1991: , , F.Cu at (185.7, 138.7)
- added 1992: , , F.Cu at (188.3, 138.7)
- added 1993: , , F.Cu at (190.8, 138.7)
- added 1994: , , F.Cu at (193.3, 138.7)
- added 1995: , , F.Cu at (195.9, 138.7)
- added 1996: , , F.Cu at (198.4, 138.7)
- added 1997: , , F.Cu at (201.0, 138.7)
- added 1998: , , F.Cu at (203.5, 138.7)
- added 1999: , , F.Cu at (206.0, 138.7)
- added 2: , , F.Cu at (162.9, 54.9)
- added 20: , , F.Cu at (208.6, 54.9)
- added 200: , , F.Cu at (208.6, 62.5)
- added 2000: , , F.Cu at (208.6, 138.7)
- added 2001: , , F.Cu at (211.1, 138.7)
- added 2002: , , F.Cu at (213.7, 138.7)
- added 2003: , , F.Cu at (216.2, 138.7)
- added 2004: , , F.Cu at (218.7, 138.7)
- added 2005: , , F.Cu at (221.3, 138.7)
- added 2006: , , F.Cu at (223.8, 138.7)
- added 2007: , , F.Cu at (226.4, 138.7)
- added 2008: , , F.Cu at (228.9, 138.7)
- added 2009: , , F.Cu at (231.4, 138.7)
- added 201: , , F.Cu at (211.1, 62.5)
- added 2010: , , F.Cu at (234.0, 138.7)
- added 2011: , , F.Cu at (236.5, 138.7)
- added 2012: , , F.Cu at (239.1, 138.7)
- added 2013: , , F.Cu at (241.6, 138.7)
- added 2014: , , F.Cu at (244.1, 138.7)
- added 2015: , , F.Cu at (246.7, 138.7)
- added 2016: , , F.Cu at (249.2, 138.7)
- added 2017: , , F.Cu at (251.8, 138.7)
- added 202: , , F.Cu at (213.7, 62.5)
- added 203: , , F.Cu at (216.2, 62.5)
- added 204: , , F.Cu at (218.7, 62.5)
- added 2042: , , F.Cu at (162.9, 141.3)
- added 2043: , , F.Cu at (165.4, 141.3)
- added 2044: , , F.Cu at (167.9, 141.3)
- added 2045: , , F.Cu at (170.5, 141.3)
- added 2046: , , F.Cu at (173.0, 141.3)
- added 2047: , , F.Cu at (175.6, 141.3)
- added 2048: , , F.Cu at (178.1, 141.3)
- added 2049: , , F.Cu at (180.6, 141.3)
- added 205: , , F.Cu at (221.3, 62.5)
- added 2050: , , F.Cu at (183.2, 141.3)
- added 2051: , , F.Cu at (185.7, 141.3)
- added 2052: , , F.Cu at (188.3, 141.3)
- added 2053: , , F.Cu at (190.8, 141.3)
- added 2054: , , F.Cu at (193.3, 141.3)
- added 2055: , , F.Cu at (195.9, 141.3)
- added 2056: , , F.Cu at (198.4, 141.3)
- added 2057: , , F.Cu at (201.0, 141.3)
- added 2058: , , F.Cu at (203.5, 141.3)
- added 2059: , , F.Cu at (206.0, 141.3)
- added 206: , , F.Cu at (223.8, 62.5)
- added 2060: , , F.Cu at (208.6, 141.3)
- added 2061: , , F.Cu at (211.1, 141.3)
- added 2062: , , F.Cu at (213.7, 141.3)
- added 2063: , , F.Cu at (216.2, 141.3)
- added 2064: , , F.Cu at (218.7, 141.3)
- added 2065: , , F.Cu at (221.3, 141.3)
- added 2066: , , F.Cu at (223.8, 141.3)
- added 2067: , , F.Cu at (226.4, 141.3)
- added 2068: , , F.Cu at (228.9, 141.3)
- added 2069: , , F.Cu at (231.4, 141.3)
- added 207: , , F.Cu at (226.4, 62.5)
- added 2070: , , F.Cu at (234.0, 141.3)
- added 2071: , , F.Cu at (236.5, 141.3)
- added 2072: , , F.Cu at (239.1, 141.3)
- added 2073: , , F.Cu at (241.6, 141.3)
- added 2074: , , F.Cu at (244.1, 141.3)
- added 2075: , , F.Cu at (246.7, 141.3)
- added 2076: , , F.Cu at (249.2, 141.3)
- added 2077: , , F.Cu at (251.8, 141.3)
- added 208: , , F.Cu at (228.9, 62.5)
- added 209: , , F.Cu at (231.4, 62.5)
- added 21: , , F.Cu at (211.1, 54.9)
- added 210: , , F.Cu at (234.0, 62.5)
- added 2102: , , F.Cu at (162.9, 143.8)
- added 2103: , , F.Cu at (165.4, 143.8)
- added 2104: , , F.Cu at (167.9, 143.8)
- added 2105: , , F.Cu at (170.5, 143.8)
- added 2106: , , F.Cu at (173.0, 143.8)
- added 2107: , , F.Cu at (175.6, 143.8)
- added 2108: , , F.Cu at (178.1, 143.8)
- added 2109: , , F.Cu at (180.6, 143.8)
- added 211: , , F.Cu at (236.5, 62.5)
- added 2110: , , F.Cu at (183.2, 143.8)
- added 2111: , , F.Cu at (185.7, 143.8)
- added 2112: , , F.Cu at (188.3, 143.8)
- added 2113: , , F.Cu at (190.8, 143.8)
- added 2114: , , F.Cu at (193.3, 143.8)
- added 2115: , , F.Cu at (195.9, 143.8)
- added 2116: , , F.Cu at (198.4, 143.8)
- added 2117: , , F.Cu at (201.0, 143.8)
- added 2118: , , F.Cu at (203.5, 143.8)
- added 2119: , , F.Cu at (206.0, 143.8)
- added 212: , , F.Cu at (239.1, 62.5)
- added 2120: , , F.Cu at (208.6, 143.8)
- added 2121: , , F.Cu at (211.1, 143.8)
- added 2122: , , F.Cu at (213.7, 143.8)
- added 2123: , , F.Cu at (216.2, 143.8)
- added 2124: , , F.Cu at (218.7, 143.8)
- added 2125: , , F.Cu at (221.3, 143.8)
- added 2126: , , F.Cu at (223.8, 143.8)
- added 2127: , , F.Cu at (226.4, 143.8)
- added 2128: , , F.Cu at (228.9, 143.8)
- added 2129: , , F.Cu at (231.4, 143.8)
- added 213: , , F.Cu at (241.6, 62.5)
- added 2130: , , F.Cu at (234.0, 143.8)
- added 2131: , , F.Cu at (236.5, 143.8)
- added 2132: , , F.Cu at (239.1, 143.8)
- added 2133: , , F.Cu at (241.6, 143.8)
- added 2134: , , F.Cu at (244.1, 143.8)
- added 2135: , , F.Cu at (246.7, 143.8)
- added 2136: , , F.Cu at (249.2, 143.8)
- added 2137: , , F.Cu at (251.8, 143.8)
- added 214: , , F.Cu at (244.1, 62.5)
- added 215: , , F.Cu at (246.7, 62.5)
- added 216: , , F.Cu at (249.2, 62.5)
- added 217: , , F.Cu at (251.8, 62.5)
- added 22: , , F.Cu at (213.7, 54.9)
- added 23: , , F.Cu at (216.2, 54.9)
- added 24: , , F.Cu at (218.7, 54.9)
- added 242: , , F.Cu at (162.9, 65.1)
- added 243: , , F.Cu at (165.4, 65.1)
- added 244: , , F.Cu at (167.9, 65.1)
- added 245: , , F.Cu at (170.5, 65.1)
- added 246: , , F.Cu at (173.0, 65.1)
- added 247: , , F.Cu at (175.6, 65.1)
- added 248: , , F.Cu at (178.1, 65.1)
- added 249: , , F.Cu at (180.6, 65.1)
- added 25: , , F.Cu at (221.3, 54.9)
- added 250: , , F.Cu at (183.2, 65.1)
- added 251: , , F.Cu at (185.7, 65.1)
- added 252: , , F.Cu at (188.3, 65.1)
- added 253: , , F.Cu at (190.8, 65.1)
- added 254: , , F.Cu at (193.3, 65.1)
- added 255: , , F.Cu at (195.9, 65.1)
- added 256: , , F.Cu at (198.4, 65.1)
- added 257: , , F.Cu at (201.0, 65.1)
- added 258: , , F.Cu at (203.5, 65.1)
- added 259: , , F.Cu at (206.0, 65.1)
- added 26: , , F.Cu at (223.8, 54.9)
- added 260: , , F.Cu at (208.6, 65.1)
- added 261: , , F.Cu at (211.1, 65.1)
- added 262: , , F.Cu at (213.7, 65.1)
- added 263: , , F.Cu at (216.2, 65.1)
- added 264: , , F.Cu at (218.7, 65.1)
- added 265: , , F.Cu at (221.3, 65.1)
- added 266: , , F.Cu at (223.8, 65.1)
- added 267: , , F.Cu at (226.4, 65.1)
- added 268: , , F.Cu at (228.9, 65.1)
- added 269: , , F.Cu at (231.4, 65.1)
- added 27: , , F.Cu at (226.4, 54.9)
- added 270: , , F.Cu at (234.0, 65.1)
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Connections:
- U13 pad 1: /Contador BCD UP/Q_{1} -> /Contador BCD UP/Q_{2}
- U13 pad 10: /Contador BCD UP/~{Q_{3}} -> /Contador BCD UP/Q_{0}
- U13 pad 2: /Contador BCD UP/Q_{0} -> /Contador BCD UP/J_{2}
- U13 pad 3: /Contador BCD UP/J_{2} -> /Contador BCD UP/J_{3}
- U13 pad 4: /Contador BCD UP/Q_{2} -> /Contador BCD UP/Q_{0}
- U13 pad 5: /Contador BCD UP/J_{2} -> /Contador BCD UP/~{Q_{3}}
- U13 pad 6: /Contador BCD UP/J_{3} -> /Contador BCD UP/J_{1}
- U13 pad 8: /Contador BCD UP/J_{1} -> /Contador BCD UP/J_{2}
- U13 pad 9: /Contador BCD UP/Q_{0} -> /Contador BCD UP/Q_{1}
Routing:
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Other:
- board size 100 x 100 mm -> 202.7 x 100.1 mm
